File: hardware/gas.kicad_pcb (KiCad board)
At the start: 2 copper layers, 65 x 30 mm, 29 parts, among them P1 CON-SENSOR2, P2 DEBUG, P3 BOOT, P4 Gas Sensor, U1 XMC1300, U2 DRILL, U3 DRILL, U4 DRILL, U5 DRILL

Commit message: all new design
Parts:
- removed Fiducial_Mark (x5): VAL**, kicad-libraries:Fiducial_Mark
- removed G***: LOGO, kicad-libraries:Logo_31x31
- removed G***: LOGO, kicad-libraries:Logo_CoMCU
- removed REF**: WA-SMSI-M3-SPACER, kicad-libraries:WA-SMSI-M3-SPACER
- removed VAL: WEEE_7mm, kicad-libraries:WEEE_7mm
- removed VAL: CE_5mm, kicad-libraries:CE_5mm
- added C10: 100nF, kicad-libraries:C0603F, F.Cu at (135.9, 109.9)
- added C7: 100nF, kicad-libraries:C0603F, F.Cu at (186.4, 119.7)
- added C8: 10uF TPSA106K010R0900, kicad-libraries:C0805P, F.Cu at (141.6, 117.4)
- added C9: DNP, kicad-libraries:R0402F, F.Cu at (143.0, 123.0)
- added P10: 3, kicad-libraries:SolderJumper, F.Cu at (133.0, 141.7)
- added P5: WORK, kicad-libraries:THT-2-2mm, F.Cu at (160.0, 140.0)
- added P6: GND, kicad-libraries:THT-2-2mm, F.Cu at (151.1, 131.1)
- added P7: 0, kicad-libraries:SolderJumper, F.Cu at (132.9, 136.3)
- added P8: 1, kicad-libraries:SolderJumper, F.Cu at (132.9, 138.1)
- added P9: 2, kicad-libraries:SolderJumper, F.Cu at (132.9, 139.9)
- added R2: 1k, kicad-libraries:R0603F, F.Cu at (141.5, 120.5)
- added R3: 499k, kicad-libraries:R0402F, F.Cu at (143.0, 124.1)
- added R4: 49,9, kicad-libraries:R0402F, F.Cu at (140.5, 123.6)
- added U10: MCP3423, kicad-libraries:MSOP10-0.5, F.Cu at (132.9, 111.9)
- added U6: HDC1080, kicad-libraries:DFN6-30x30_humidity, F.Cu at (184.2, 119.7)
- added U7: ISL60002, kicad-libraries:SOT23-3, F.Cu at (139.2, 118.8)
- added U8: LMP91000, kicad-libraries:WSON-14-LMP91000, F.Cu at (142.2, 127.5)
- added U9: MCP6041, kicad-libraries:SOT23-5, F.Cu at (146.2, 127.5)
- C5: value 10uF -> 100nF; footprint kicad-libraries:C0805 -> kicad-libraries:C0603F
- C6: value 100n -> 100nF
- P4: value Gas Sensor -> RC; footprint kicad-libraries:pin_array_8x1_smd -> kicad-libraries:THT-2-2mm
- RP2: value 100 -> 10k; footprint kicad-libraries:4X0402 -> kicad-libraries:0603X4
- moved U3 70.9 mm to (192.5, 118.6)
- moved U5 65.8 mm to (127.5, 118.6)
- moved U2 61.4 mm to (127.5, 143.6)
- moved C5 57.3 mm to (143.5, 131.0), turned to 0 degrees
- moved C6 54.8 mm to (139.3, 121.2), turned to 180 degrees
- moved RP2 51.0 mm to (181.0, 129.1), turned to 0 degrees
- moved C3 42.5 mm to (133.5, 128.6), turned to 270 degrees
- moved C2 42.4 mm to (131.9, 128.6), turned to 270 degrees
- moved P2 41.8 mm to (134.6, 144.3), turned to 0 degrees
- moved P3 39.9 mm to (133.0, 144.3), turned to 90 degrees
- moved U4 37.5 mm to (192.5, 143.6)
- moved C4 36.5 mm to (138.0, 143.7)
- moved P1 36.5 mm to (125.0, 131.1)
- moved R1 36.1 mm to (146.5, 143.4), turned to 90 degrees
- moved U1 36.0 mm to (138.0, 139.7)
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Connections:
- C5 pad 1: GND -> VCC
- C5 pad 2: VCC -> GND
- C6 pad 1: VCC -> Net-(C6-Pad1)
- RP2 pad 1: Net-(RP2-Pad1) -> VCC
- RP2 pad 2: GS_RX -> Net-(RP2-Pad2)
- RP2 pad 3: GS_TX -> Net-(RP2-Pad3)
- RP2 pad 4: Net-(RP2-Pad4) -> VCC
- RP2 pad 5: Net-(RP2-Pad5) -> SCL0
- RP2 pad 6: Net-(P4-Pad2) -> Net-(RP2-Pad6)
- RP2 pad 7: Net-(P4-Pad3) -> Net-(RP2-Pad7)
- RP2 pad 8: Net-(RP2-Pad8) -> SDA0
- U1 pad 17: GS_TX -> SDA0
- U1 pad 18: GS_RX -> Net-(U1-Pad18)
- U1 pad 19: Net-(U1-Pad19) -> SCL0
- U1 pad 2: Net-(P2-Pad1) -> SolderJumper0
- U1 pad 20: Net-(U1-Pad20) -> Enable
- U1 pad 3: Net-(U1-Pad3) -> SolderJumper1
- U1 pad 4: Net-(U1-Pad4) -> SolderJumper2
- U1 pad 5: Net-(P3-Pad2) -> SolderJumper3
- U1 pad 6: Net-(U1-Pad6) -> Net-(P3-Pad2)
- U1 pad 7: Net-(U1-Pad7) -> Net-(P2-Pad1)
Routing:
- net VCC: track 121.9 -> 0.00 mm, vias 2 -> 0
- net Net-(P4-Pad3): track 43.0 -> 0.00 mm
- net Net-(P4-Pad2): track 42.8 -> 0.00 mm
- net GND: track 31.4 -> 0.00 mm, vias 12 -> 0
- net Net-(R1-Pad1): track 25.5 -> 0.00 mm
- net Net-(P1-Pad4): track 7.43 -> 0.00 mm
- net Net-(P1-Pad5): track 5.62 -> 0.00 mm
- net S-MISO: track 4.96 -> 0.00 mm
- net S-CLK: track 4.87 -> 0.00 mm
- net Net-(C1-Pad1): track 4.83 -> 0.00 mm
- net S-MOSI: track 4.70 -> 0.00 mm
- net S-CS: track 4.69 -> 0.00 mm
- net Net-(P1-Pad6): track 4.48 -> 0.00 mm
- net Net-(P2-Pad1): track 4.33 -> 0.00 mm
- net Net-(P3-Pad2): track 4.12 -> 0.00 mm
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- removed copper zone on B.Cu, net GND
- removed copper zone on F.Cu, net GND
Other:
- board size 65 x 30 mm -> 70 x 30 mm
- net class Default: clearance 0.149 -> 0.2
- rule trace_clearance: 0.149 -> 0.2
- rule trace_min: 0.1 -> 0.2
- rule via_min_drill: 0.25 -> 0.3
- board text removed: "Gas 1.0"
- board text removed: "Status"
- board text removed: "tinkerforge.com"

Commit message: changes in pcb design
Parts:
- removed P4: RC, kicad-libraries:THT-2-2mm
- removed P5: WORK, kicad-libraries:THT-2-2mm
- removed P6: GND, kicad-libraries:THT-2-2mm
- added C11: 100nF, kicad-libraries:C0603F, F.Cu at (146.0, 139.4)
- added C12: 100nF, kicad-libraries:C0603F, F.Cu at (141.6, 130.0)
- added U11: spec-sensor, kicad-libraries:spec-sensor, F.Cu at (159.0, 131.1)
- moved C7 52.7 mm to (133.8, 119.8), turned to 90 degrees
- moved U6 47.8 mm to (136.4, 119.8), turned to 0 degrees
- moved RP2 42.7 mm to (138.4, 132.5), turned to 90 degrees
- moved C10 24.9 mm to (145.9, 132.7)
- moved U10 21.4 mm to (145.9, 128.9), turned to 180 degrees
- moved C8 21.1 mm to (143.7, 138.4), turned to 270 degrees
- moved U3 20.0 mm to (172.5, 118.6)
- moved U4 20.0 mm to (172.5, 143.6)
- moved U7 19.8 mm to (146.8, 137.1), turned to 0 degrees
- moved C6 15.2 mm to (146.7, 134.5), turned to 0 degrees
- moved R2 14.9 mm to (143.7, 135.3), turned to 90 degrees
- moved C5 7.33 mm to (138.7, 125.5), turned to 270 degrees
- moved R4 5.54 mm to (145.8, 122.0), turned to 180 degrees
- moved U9 4.21 mm to (142.0, 127.8), turned to 90 degrees
- moved U8 3.76 mm to (142.0, 123.8), turned to 270 degrees
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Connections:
- P10 pad 1: Net-(P10-Pad1) -> GND
- P7 pad 1: Net-(P10-Pad1) -> GND
- P8 pad 1: Net-(P10-Pad1) -> GND
- P9 pad 1: Net-(P10-Pad1) -> GND
- RP2 pad 2: Net-(RP2-Pad2) -> VCC
- RP2 pad 3: Net-(RP2-Pad3) -> VCC
- U10 pad 4: Net-(U10-Pad4) -> GND
- U10 pad 5: Net-(U10-Pad5) -> GND
- U8 pad 1: (no net) -> GND
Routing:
- net VCC: track 0.00 -> 68.6 mm
- net Net-(U11-Pad1): track 0.00 -> 32.5 mm
- net SDA0: track 0.00 -> 32.4 mm, vias 0 -> 4
- net GND: track 0.00 -> 29.2 mm, vias 0 -> 1
- net SCL0: track 0.00 -> 29.1 mm, vias 0 -> 3
- net Enable: track 0.00 -> 20.2 mm, vias 0 -> 2
- net Net-(C6-Pad1): track 0.00 -> 20.1 mm
- net Net-(R4-Pad1): track 0.00 -> 15.1 mm
- net Net-(U11-Pad4): track 0.00 -> 14.3 mm
- net Net-(U10-Pad2): track 0.00 -> 11.6 mm
- net S-CS: track 0.00 -> 6.33 mm
- net S-CLK: track 0.00 -> 5.63 mm
- net S-MOSI: track 0.00 -> 4.85 mm
- net S-MISO: track 0.00 -> 4.74 mm
- net Net-(C1-Pad1): track 0.00 -> 3.99 mm
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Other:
- board size 70 x 30 mm -> 50 x 30 mm
- net class Default: clearance 0.2 -> 0.149
- rule trace_clearance: 0.2 -> 0.149
- rule trace_min: 0.2 -> 0.1
- rule via_min_drill: 0.3 -> 0.24

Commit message: final prototype
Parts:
- added G***: LOGO, kicad-libraries:Logo_31x31, F.Cu at (154.1, 143.9)
- added G***: LOGO, kicad-libraries:Logo_CoMCU, B.Cu at (145.0, 131.1)
- added VAL: WEEE_7mm, kicad-libraries:WEEE_7mm, B.Cu at (138.0, 131.1)
- added VAL: CE_5mm, kicad-libraries:CE_5mm, B.Cu at (131.0, 131.1)
- moved P3 4.60 mm to (137.6, 144.6)
- moved P2 4.45 mm to (139.1, 145.0)
- moved C12 2.47 mm to (139.6, 128.6), turned to 90 degrees
- moved P10 2.11 mm to (132.8, 143.8)
- moved R4 1.88 mm to (144.4, 120.8)
- moved P9 1.40 mm to (132.8, 141.3)
- moved P8 0.71 mm to (132.8, 138.8)
- moved U8 0.35 mm to (142.0, 123.4)
- moved C9 0.25 mm to (146.1, 124.6)
- moved R3 0.25 mm to (145.0, 124.6)
- moved P7 0.10 mm to (132.8, 136.3)
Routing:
- net GND: track 29.2 -> 67.7 mm, vias 1 -> 22
- net Net-(U11-Pad1): track 32.5 -> 25.1 mm
- net Net-(P2-Pad1): track 0.00 -> 7.15 mm
- net SolderJumper3: track 0.00 -> 7.04 mm
- net Net-(P3-Pad2): track 0.00 -> 6.43 mm
- net Net-(R1-Pad1): track 0.00 -> 6.21 mm, vias 0 -> 2
- net SolderJumper2: track 0.00 -> 4.89 mm
- net SolderJumper0: track 0.00 -> 3.53 mm
- net SolderJumper1: track 0.00 -> 3.24 mm
- net VCC: track 68.6 -> 71.5 mm
- net Net-(D1-Pad2): track 0.00 -> 1.54 mm
- net Net-(R4-Pad2): track 1.48 -> 0.00 mm
- net Net-(R4-Pad1): track 15.1 -> 16.2 mm
- net Enable: track 20.2 -> 19.1 mm
- net Net-(U11-Pad4): track 14.3 -> 13.3 mm
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- added copper zone on B.Cu, net GND
- added copper zone on F.Cu, net GND
- added copper zone on F.Cu, net Net-(R4-Pad2)
- added copper zone on F.Cu, net Net-(U11-Pad1)
- added copper zone on F.Cu, net Net-(U11-Pad4)
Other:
- outline, holes or cut-outs redrawn
- board text added: "0"
- board text added: "1"
- board text added: "2"
- board text added: "3"
- board text added: "Gas 1.0"
- board text added: "Status"
- board text added: "tinkerforge.com"

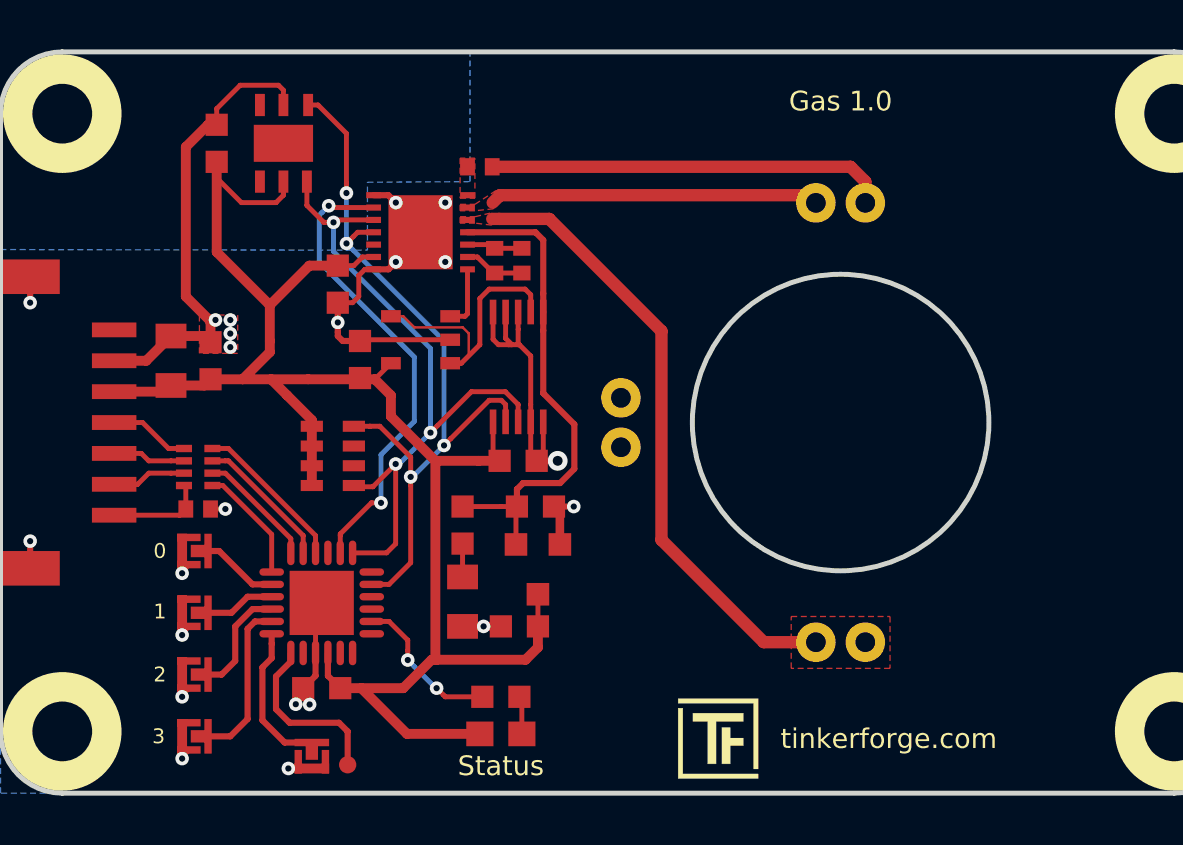
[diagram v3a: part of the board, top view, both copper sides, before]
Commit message: corrected wrong pinout of ISL60002 in schematic and pcb design
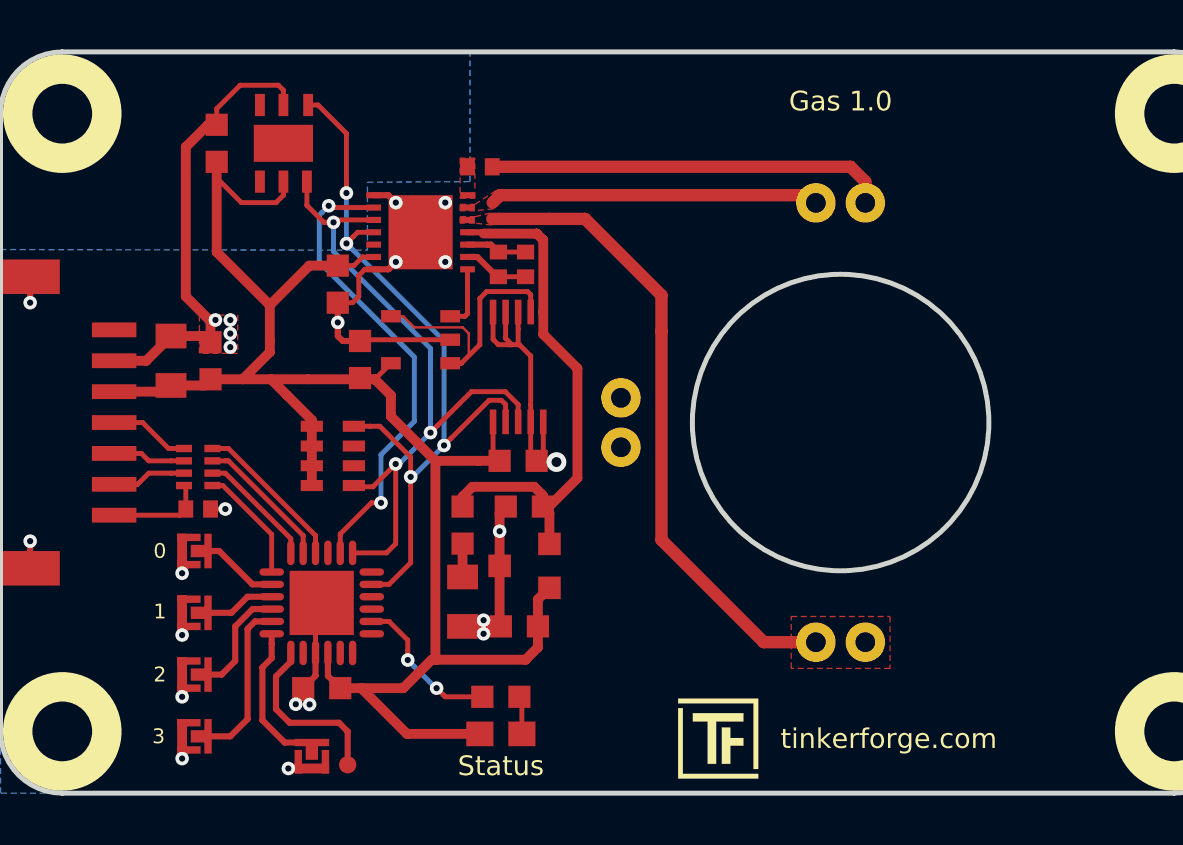
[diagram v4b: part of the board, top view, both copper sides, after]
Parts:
- moved U7 0.57 mm to (146.2, 136.9), turned to 270 degrees
- moved C6 0.45 mm to (146.2, 134.5), turned to 180 degrees
- moved C9 0.21 mm to (146.2, 124.7)
- moved R3 0.21 mm to (145.2, 124.7)
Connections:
- U7 pad 1: GND -> VCC
- U7 pad 3: VCC -> GND
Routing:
- net GND: track 67.7 -> 72.2 mm, vias 22 -> 23
- net Net-(C6-Pad1): track 20.1 -> 21.3 mm
- net Net-(U11-Pad1): track 25.1 -> 26.0 mm

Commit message: drc check
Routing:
- net Net-(C6-Pad1): track 21.3 -> 19.8 mm
- added copper zone on F.Cu, net Net-(C6-Pad1)
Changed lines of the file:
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@@
     (thickness 1.6)
     (drawings 16)
-    (tracks 403)
+    (tracks 395)
     (zones 0)
     (modules 41)
@@
   (segment (start 143.19888 126.81004) (end 143.79893 126.81004) (width 0.2) (layer F.Cu) (net 36))
   (segment (start 143.79893 126.81004) (end 143.9 126.70897) (width 0.2) (layer F.Cu) (net 36))
-  (segment (start 144.499434 123.41) (end 143.9 123.41) (width 0.25) (layer F.Cu) (net 37))
-  (segment (start 144.55 123.460566) (end 144.499434 123.41) (width 0.25) (layer F.Cu) (net 37))
   (segment (start 147.216 134.776) (end 146.95 134.51) (width 0.4) (layer F.Cu) (net 37))
   (segment (start 147.216 136.021) (end 147.216 134.776) (width 0.4) (layer F.Cu) (net 37))
@@
   (segment (start 146.966 126.6375) (end 146.966 127.53788) (width 0.4) (layer F.Cu) (net 37))
   (segment (start 146.966 127.53788) (end 148.349002 128.920882) (width 0.4) (layer F.Cu) (net 37))
-  (segment (start 146.708019 123.468019) (end 146.700566 123.468019) (width 0.4) (layer F.Cu) (net 37))
-  (segment (start 146.966 123.726) (end 146.708019 123.468019) (width 0.4) (layer F.Cu) (net 37))
-  (segment (start 146.966 126.6375) (end 146.966 123.726) (width 0.4) (layer F.Cu) (net 37))
-  (segment (start 144.55 123.460566) (end 146.700566 123.468019) (width 0.4) (layer F.Cu) (net 37))
-  (segment (start 146.700566 123.468019) (end 146.700566 123.460566) (width 0.4) (layer F.Cu) (net 37))
+  (segment (start 146.966 123.647798) (end 146.966 126.6375) (width 0.4) (layer F.Cu) (net 37))
+  (segment (start 145.45 123.335) (end 146.653202 123.335) (width 0.4) (layer F.Cu) (net 37))
+  (segment (start 146.653202 123.335) (end 146.966 123.647798) (width 0.4) (layer F.Cu) (net 37))
   (segment (start 143.65004 128.70996) (end 143.19888 128.70996) (width 0.1) (layer F.Cu) (net 38))
   (segment (start 141.30117 126.81004) (end 141.75113 127.26) (width 0.1) (layer F.Cu) (net 38))
@@
   (segment (start 144.9 120.76) (end 159.4 120.76) (width 0.5) (layer F.Cu) (net 43))
   (segment (start 159.4 120.76) (end 160 121.36) (width 0.5) (layer F.Cu) (net 43))
-  (segment (start 145.178829 122.869009) (end 144.9 122.869009) (width 0.5) (layer F.Cu) (net 44))
-  (segment (start 147.209009 122.869009) (end 145.178829 122.869009) (width 0.5) (layer F.Cu) (net 44))
-  (segment (start 151.75 135.86) (end 151.75 127.41) (width 0.5) (layer F.Cu) (net 44))
-  (segment (start 158 140) (end 155.89 140) (width 0.5) (layer F.Cu) (net 44))
-  (segment (start 155.89 140) (end 151.75 135.86) (width 0.5) (layer F.Cu) (net 44))
-  (segment (start 147.209009 122.869009) (end 148.659009 122.869009) (width 0.5) (layer F.Cu) (net 44))
-  (segment (start 151.75 125.96) (end 151.75 127.41) (width 0.5) (layer F.Cu) (net 44))
-  (segment (start 148.659009 122.869009) (end 151.75 125.96) (width 0.5) (layer F.Cu) (net 44))
-  (segment (start 145.22 121.91) (end 144.91901 122.21099) (width 0.5) (layer F.Cu) (net 45))
+  (segment (start 155.89 140) (end 158 140) (width 0.5) (layer F.Cu) (net 44))
+  (segment (start 151.75 135.86) (end 155.89 140) (width 0.5) (layer F.Cu) (net 44))
+  (segment (start 151.75 125.96) (end 151.75 135.86) (width 0.5) (layer F.Cu) (net 44))
+  (segment (start 145.4 122.56) (end 148.35 122.56) (width 0.5) (layer F.Cu) (net 44))
+  (segment (start 148.35 122.56) (end 151.75 125.96) (width 0.5) (layer F.Cu) (net 44))
+  (segment (start 157.69 121.91) (end 145.22 121.91) (width 0.5) (layer F.Cu) (net 45))
   (segment (start 158 122.22) (end 157.69 121.91) (width 0.5) (layer F.Cu) (net 45))
-  (segment (start 157.69 121.91) (end 145.22 121.91) (width 0.5) (layer F.Cu) (net 45))
   (zone (net 44) (net_name "Net-(U11-Pad1)") (layer F.Cu) (hatch edge 0.508)
     (connect_pads yes (clearance 0.508))
@@
     (connect_pads yes (clearance 0.001))
     (min_thickness 0.1)
-    (fill yes (arc_segments 16) (thermal_gap 0.508) (thermal_bridge_width 0.508))
+    (fill yes (arc_segments 16) (thermal_gap 0.149) (thermal_bridge_width 0.508))
     (polygon
       (pts
-        (xy 143.6 122.28) (xy 144.2 122.28) (xy 145.15 121.66) (xy 144.95 122.46) (xy 144.2 122.54)
+        (xy 143.6 122.28) (xy 144.2 122.28) (xy 145.15 121.66) (xy 145.3 122.16) (xy 144.2 122.54)
         (xy 143.6 122.54)
       )
@@
     (polygon
       (pts
-        (xy 143.6 122.78) (xy 144.21 122.78) (xy 144.88 122.62) (xy 144.88 123.12) (xy 144.2 123.04)
+        (xy 143.6 122.78) (xy 144.21 122.78) (xy 145.35 122.31) (xy 145.4 122.81) (xy 144.2 123.04)
         (xy 143.6 123.04)
       )
     )
+  )
+  (zone (net 37) (net_name "Net-(C6-Pad1)") (layer F.Cu) (hatch edge 0.508)
+    (connect_pads yes (clearance 0.001))
+    (min_thickness 0.1)
+    (fill yes (arc_segments 16) (thermal_gap 0.149) (thermal_bridge_width 0.508))
+    (polygon
+      (pts
+        (xy 143.85 123.285) (xy 144.2 123.285) (xy 145.425 123.135) (xy 145.425 123.535) (xy 144.2 123.535)
+        (xy 143.85 123.535)
+      )
+    )
